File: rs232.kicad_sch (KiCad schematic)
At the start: 7 parts, among them J17 RS-232 DE9 (M,DTE), U11 MAX3232E

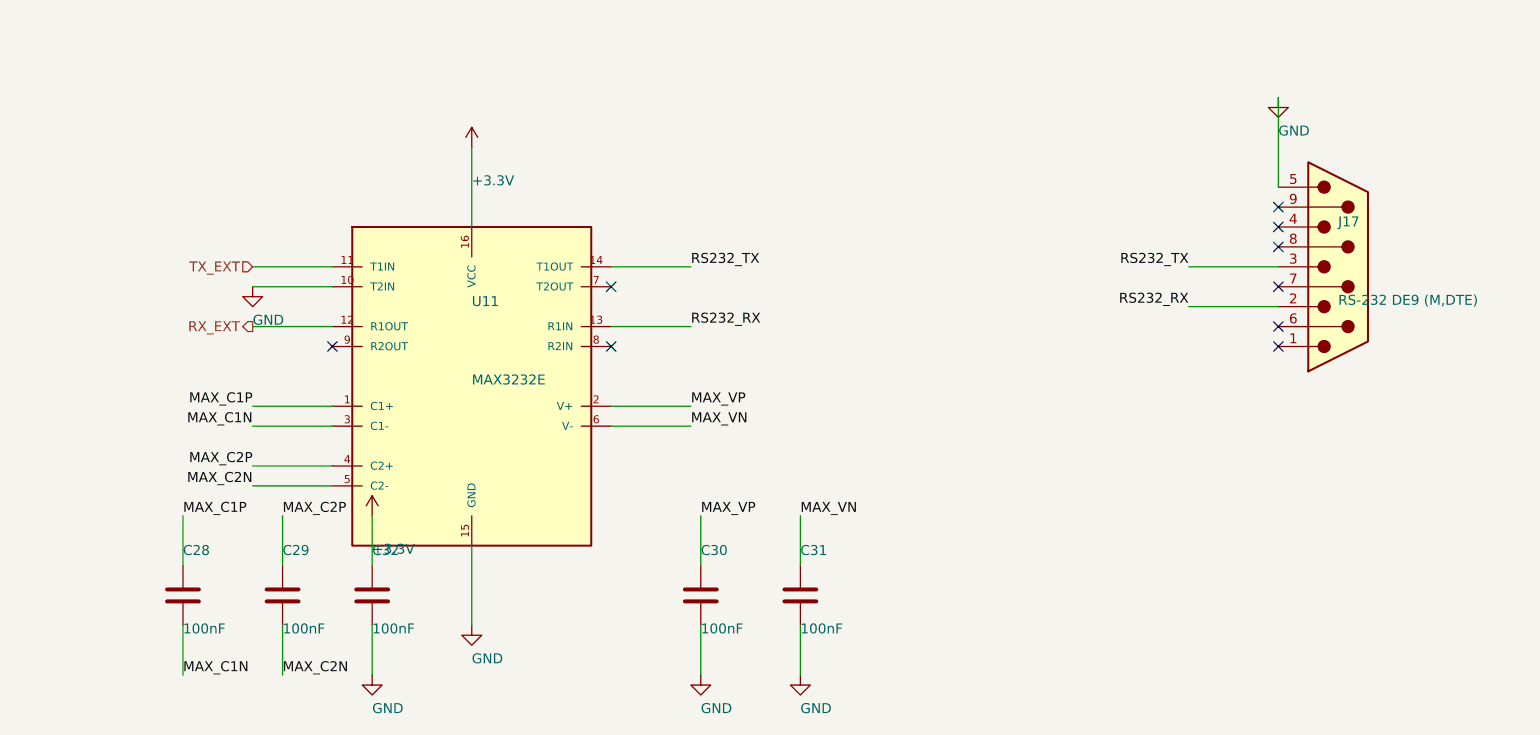
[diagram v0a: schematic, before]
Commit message: WIP: J18/Q2/Q3/R30/R31 + reguardado KiCad de todas las hojas
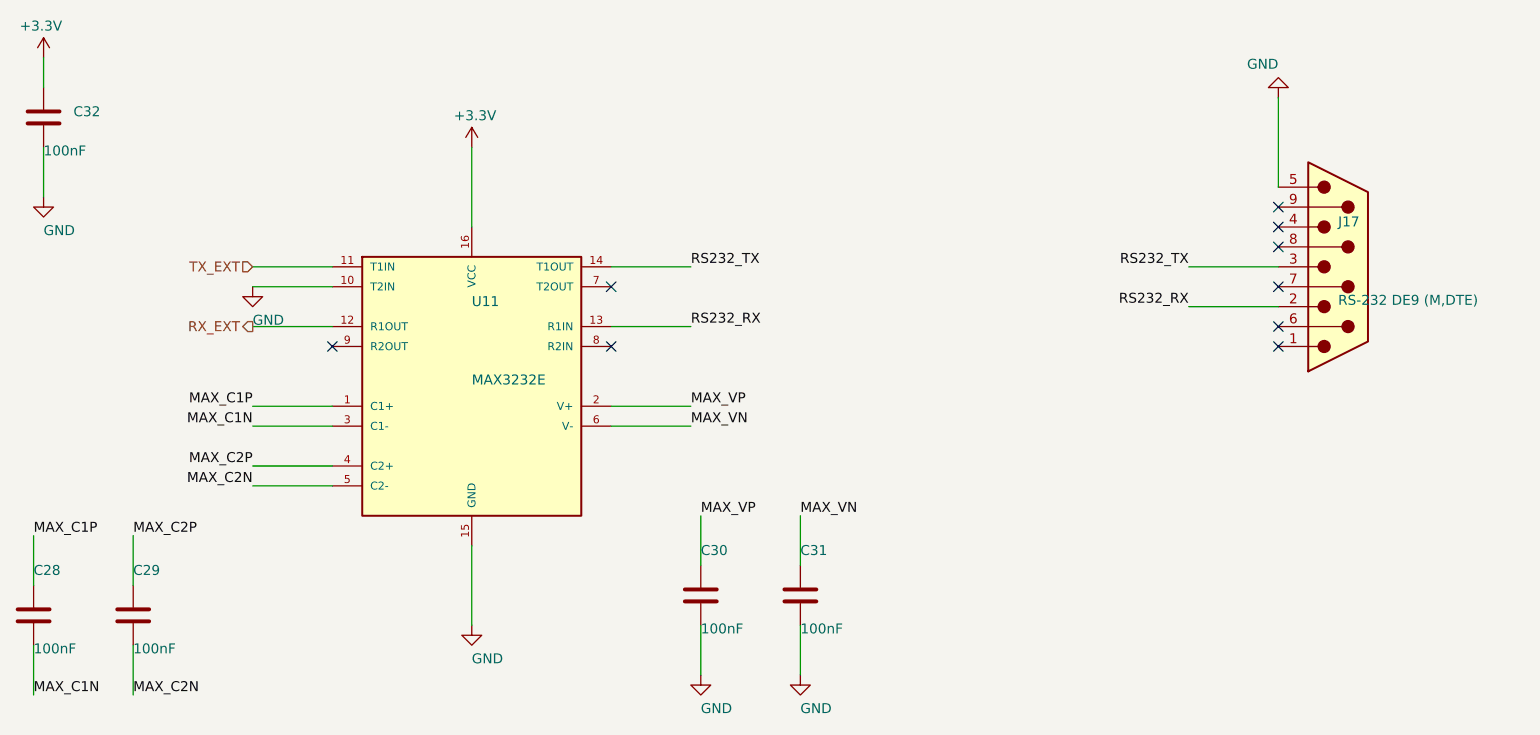
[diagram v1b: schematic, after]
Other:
- moved on the sheet: C28, C29, C32

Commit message: friday changes
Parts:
- C28, C29, C30, C31, C32: DigiKey (none) -> 1276-1003-2-ND; MPN (none) -> CL21B104KBCNNNC; Manufacturer (none) -> Samsung Electro-Mechanics
- J17: DigiKey (none) -> L717SDE09PA4CH4F-ND
- U11: DigiKey (none) -> 296-19752-2-ND
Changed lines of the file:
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@@
+			)
+		)
+		(property "DigiKey" "296-19752-2-ND"
+			(at 0 0 0)
+			(effects
+				(font
+					(size 1.27 1.27)
+				)
+				(hide yes)
 			)
 		)
@@
 			)
 		)
+		(property "Manufacturer" "Samsung Electro-Mechanics"
+			(at 0 0 0)
+			(effects
+				(font
+					(size 1.27 1.27)
+				)
+				(hide yes)
+			)
+		)
+		(property "MPN" "CL21B104KBCNNNC"
+			(at 0 0 0)
+			(effects
+				(font
+					(size 1.27 1.27)
+				)
+				(hide yes)
+			)
+		)
+		(property "DigiKey" "1276-1003-2-ND"
+			(at 0 0 0)
+			(effects
+				(font
+					(size 1.27 1.27)
+				)
+				(hide yes)
+			)
+		)
 		(pin "1"
 		)
@@
 			)
 		)
+		(property "Manufacturer" "Samsung Electro-Mechanics"
+			(at 0 0 0)
+			(effects
+				(font
+					(size 1.27 1.27)
+				)
+				(hide yes)
+			)
+		)
+		(property "MPN" "CL21B104KBCNNNC"
+			(at 0 0 0)
+			(effects
+				(font
+					(size 1.27 1.27)
+				)
+				(hide yes)
+			)
+		)
+		(property "DigiKey" "1276-1003-2-ND"
+			(at 0 0 0)
+			(effects
+				(font
+					(size 1.27 1.27)
+				)
+				(hide yes)
+			)
+		)
 		(pin "1"
 		)
@@
 			)
 		)
+		(property "Manufacturer" "Samsung Electro-Mechanics"
+			(at 0 0 0)
+			(effects
+				(font
+					(size 1.27 1.27)
+				)
+				(hide yes)
+			)
+		)
+		(property "MPN" "CL21B104KBCNNNC"
+			(at 0 0 0)
+			(effects
+				(font
+					(size 1.27 1.27)
+				)
+				(hide yes)
+			)
+		)
+		(property "DigiKey" "1276-1003-2-ND"
+			(at 0 0 0)
+			(effects
+				(font
+					(size 1.27 1.27)
+				)
+				(hide yes)
+			)
+		)
 		(pin "1"
 		)
@@
 			)
 		)
+		(property "Manufacturer" "Samsung Electro-Mechanics"
+			(at 0 0 0)
+			(effects
+				(font
+					(size 1.27 1.27)
+				)
+				(hide yes)
+			)
+		)
+		(property "MPN" "CL21B104KBCNNNC"
+			(at 0 0 0)
+			(effects
+				(font
+					(size 1.27 1.27)
+				)
+				(hide yes)
+			)
+		)
+		(property "DigiKey" "1276-1003-2-ND"
+			(at 0 0 0)
+			(effects
+				(font
+					(size 1.27 1.27)
+				)
+				(hide yes)
+			)
+		)
 		(pin "1"
 		)
@@
 			)
 		)
+		(property "Manufacturer" "Samsung Electro-Mechanics"
+			(at 0 0 0)
+			(effects
+				(font
+					(size 1.27 1.27)
+				)
+				(hide yes)
+			)
+		)
+		(property "MPN" "CL21B104KBCNNNC"
+			(at 0 0 0)
+			(effects
+				(font
+					(size 1.27 1.27)
+				)
+				(hide yes)
+			)
+		)
+		(property "DigiKey" "1276-1003-2-ND"
+			(at 0 0 0)
+			(effects
+				(font
+					(size 1.27 1.27)
+				)
+				(hide yes)
+			)
+		)
 		(pin "1"
 		)
@@
 				(hide yes)
 			)
+		)
+		(property "DigiKey" "L717SDE09PA4CH4F-ND"
+			(at 0 0 0)
+			(effects
+				(font
+					(size 1.27 1.27)
+				)
+				(hide yes)
+			)

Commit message: schematic updated
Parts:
- renumbered C28 to C3, C32 to C4, C29 to C5, C30 to C6, C31 to C7, J17 to J4, U11 to U2
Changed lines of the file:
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@@
 		(on_board yes)
 		(dnp no)
-		(property "Reference" "U11"
+		(property "Reference" "U2"
 			(at 90.17 66.12 0)
 			(effects
@@
 			(project "controlcarreta"
 				(path "/9232987b-e923-413e-abd9-77ced6cc4c47/a1b2c3d4-0000-4000-8000-000000052320"
-					(reference "U11")
+					(reference "U2")
 					(unit 1)
 				)
@@
 		(on_board yes)
 		(dnp no)
-		(property "Reference" "#PWR0528"
+		(property "Reference" "#PWR021"
 			(at 62.23 58.5 0)
 			(effects
@@
 			(project "controlcarreta"
 				(path "/9232987b-e923-413e-abd9-77ced6cc4c47/a1b2c3d4-0000-4000-8000-000000052320"
-					(reference "#PWR0528")
+					(reference "#PWR021")
 					(unit 1)
 				)
@@
 		(on_board yes)
 		(dnp no)
-		(property "Reference" "#PWR0529"
+		(property "Reference" "#PWR022"
 			(at 90.17 40.72 0)
 			(effects
@@
 			(project "controlcarreta"
 				(path "/9232987b-e923-413e-abd9-77ced6cc4c47/a1b2c3d4-0000-4000-8000-000000052320"
-					(reference "#PWR0529")
+					(reference "#PWR022")
 					(unit 1)
 				)
@@
 		(on_board yes)
 		(dnp no)
-		(property "Reference" "#PWR0530"
+		(property "Reference" "#PWR023"
 			(at 90.17 101.68 0)
 			(effects
@@
 			(project "controlcarreta"
 				(path "/9232987b-e923-413e-abd9-77ced6cc4c47/a1b2c3d4-0000-4000-8000-000000052320"
-					(reference "#PWR0530")
+					(reference "#PWR023")
 					(unit 1)
 				)
@@
 		(on_board yes)
 		(dnp no)
-		(property "Reference" "C28"
+		(property "Reference" "C3"
 			(at 34.29 100.41 0)
 			(effects
@@
 			(project "controlcarreta"
 				(path "/9232987b-e923-413e-abd9-77ced6cc4c47/a1b2c3d4-0000-4000-8000-000000052320"
-					(reference "C28")
+					(reference "C3")
 					(unit 1)
 				)
@@
 		(on_board yes)
 		(dnp no)
-		(property "Reference" "C29"
+		(property "Reference" "C5"
 			(at 46.99 100.41 0)
 			(effects
@@
 			(project "controlcarreta"
 				(path "/9232987b-e923-413e-abd9-77ced6cc4c47/a1b2c3d4-0000-4000-8000-000000052320"
-					(reference "C29")
+					(reference "C5")
 					(unit 1)
 				)
@@
 		(on_board yes)
 		(dnp no)
-		(property "Reference" "C32"
+		(property "Reference" "C4"
 			(at 39.37 41.91 0)
 			(effects
@@
 			(project "controlcarreta"
 				(path "/9232987b-e923-413e-abd9-77ced6cc4c47/a1b2c3d4-0000-4000-8000-000000052320"
-					(reference "C32")
+					(reference "C4")
 					(unit 1)
 				)
@@
 		(on_board yes)
 		(dnp no)
-		(property "Reference" "#PWR0531"
+		(property "Reference" "#PWR019"
 			(at 35.56 29.29 0)
 			(effects
@@
 			(project "controlcarreta"
 				(path "/9232987b-e923-413e-abd9-77ced6cc4c47/a1b2c3d4-0000-4000-8000-000000052320"
-					(reference "#PWR0531")
+					(reference "#PWR019")
 					(unit 1)
 				)
@@
 		(on_board yes)
 		(dnp no)
-		(property "Reference" "#PWR0532"
+		(property "Reference" "#PWR020"
 			(at 35.56 47.07 0)
 			(effects
@@
 			(project "controlcarreta"
 				(path "/9232987b-e923-413e-abd9-77ced6cc4c47/a1b2c3d4-0000-4000-8000-000000052320"
-					(reference "#PWR0532")
+					(reference "#PWR020")
 					(unit 1)
 				)
@@
 		(on_board yes)
 		(dnp no)
-		(property "Reference" "C30"
+		(property "Reference" "C6"
 			(at 119.38 97.87 0)
 			(effects
@@
 			(project "controlcarreta"
 				(path "/9232987b-e923-413e-abd9-77ced6cc4c47/a1b2c3d4-0000-4000-8000-000000052320"
-					(reference "C30")
+					(reference "C6")
 					(unit 1)
 				)
@@
 		(on_board yes)
 		(dnp no)
-		(property "Reference" "#PWR0533"
+		(property "Reference" "#PWR024"
 			(at 119.38 108.03 0)
 			(effects
@@
 			(project "controlcarreta"
 				(path "/9232987b-e923-413e-abd9-77ced6cc4c47/a1b2c3d4-0000-4000-8000-000000052320"
-					(reference "#PWR0533")
+					(reference "#PWR024")
 					(unit 1)
 				)
@@
 		(on_board yes)
 		(dnp no)
-		(property "Reference" "C31"
+		(property "Reference" "C7"
 			(at 132.08 97.87 0)
 			(effects
@@
 			(project "controlcarreta"
 				(path "/9232987b-e923-413e-abd9-77ced6cc4c47/a1b2c3d4-0000-4000-8000-000000052320"
-					(reference "C31")
+					(reference "C7")
 					(unit 1)
 				)
@@
 		(on_board yes)
 		(dnp no)
-		(property "Reference" "#PWR0534"
+		(property "Reference" "#PWR025"
 			(at 132.08 108.03 0)
 			(effects
@@
 			(project "controlcarreta"
 				(path "/9232987b-e923-413e-abd9-77ced6cc4c47/a1b2c3d4-0000-4000-8000-000000052320"
-					(reference "#PWR0534")
+					(reference "#PWR025")
 					(unit 1)
 				)
@@
 		(on_board yes)
 		(dnp no)
-		(property "Reference" "J17"
+		(property "Reference" "J4"
 			(at 200.66 55.96 0)
 			(effects
@@
 			(project "controlcarreta"
 				(path "/9232987b-e923-413e-abd9-77ced6cc4c47/a1b2c3d4-0000-4000-8000-000000052320"
-					(reference "J17")
+					(reference "J4")
 					(unit 1)
 				)
@@
 		(on_board yes)
 		(dnp no)
-		(property "Reference" "#PWR0535"
+		(property "Reference" "#PWR026"
 			(at 193.04 44.37 0)
 			(effects
@@
 			(project "controlcarreta"
 				(path "/9232987b-e923-413e-abd9-77ced6cc4c47/a1b2c3d4-0000-4000-8000-000000052320"
-					(reference "#PWR0535")
-					(unit 1)
-				)
+					(reference "#PWR026")
+					(unit 1)
+				)
